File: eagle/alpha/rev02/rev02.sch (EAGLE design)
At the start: 311 parts, among them CN1 HOST, IC3 N25Q128A13ES, Q3 2N7002, Q5 ASFL1, Q6 2N7002, T1 BC847, T2 BC847, T3 BC818, U1 LP3985IM5-3.3, U2 MC74HC1G14DTT1G, U3 ATTINY828R-AU, U4 MC14551BDG, U5 23K640-I/SN, U6 MCP79412-I/SN, U7 XC7A200TFBG484, Y1 12 MHz

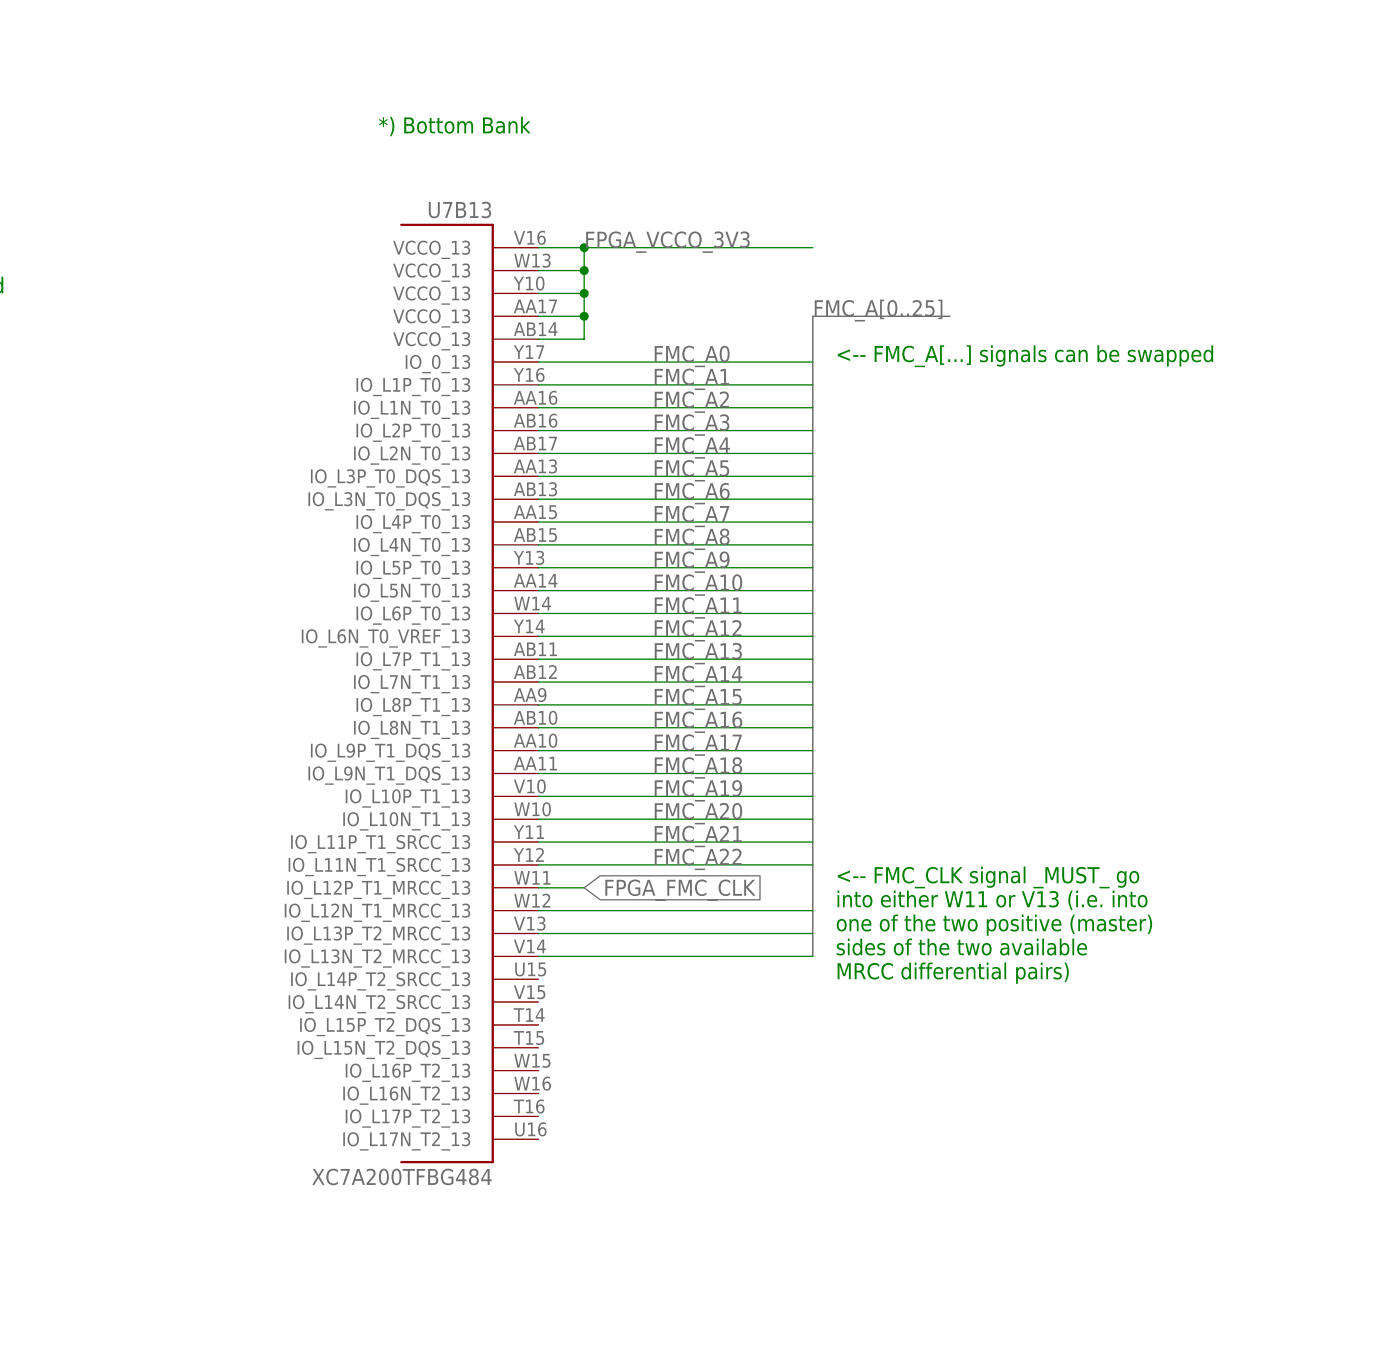
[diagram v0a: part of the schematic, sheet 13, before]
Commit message: finished merging Pavel's FPGA schematics into the dev-bridge schematics.
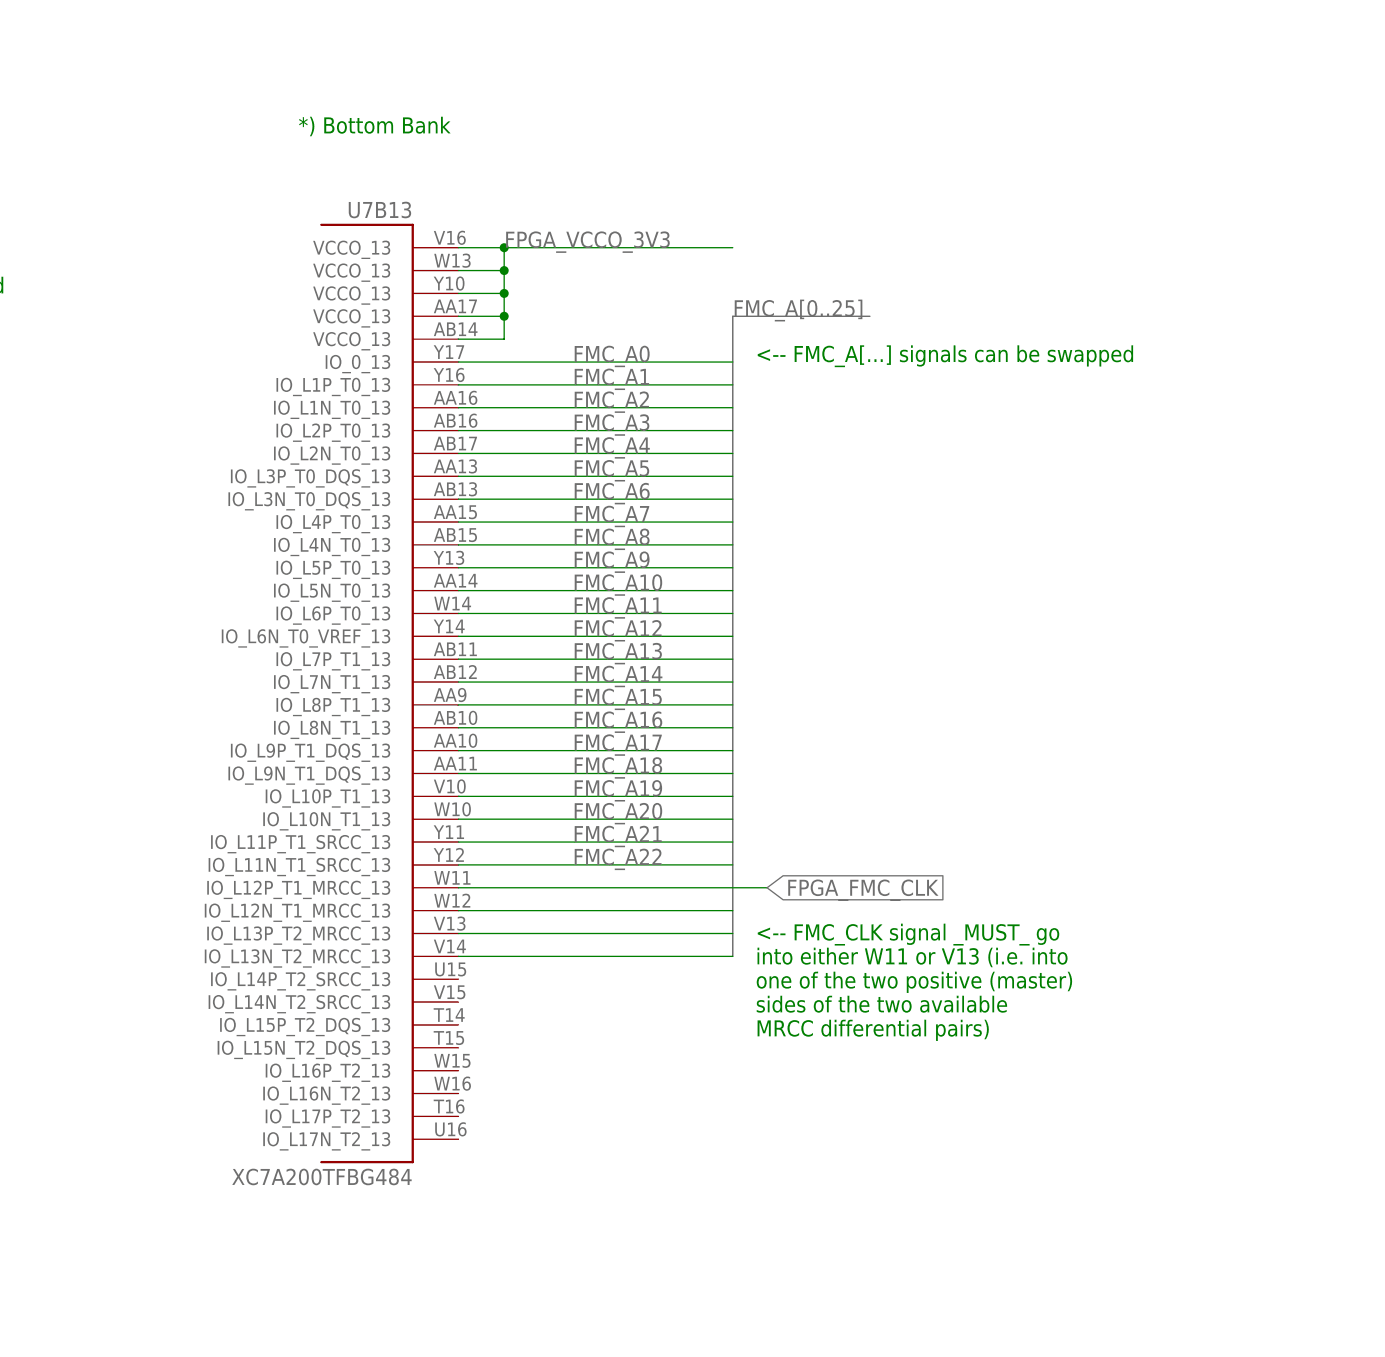
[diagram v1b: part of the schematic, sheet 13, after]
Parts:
- added C1, C4: 10NF, rcl:C-EUC0603
- added U$9: LT3060, Alpha-Power:LT3060
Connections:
- removed net DIGITIZED: U2.OUT_Y
- removed net FMC_CLK: U$1G$4.PD3/FMC_CLK
- removed net FPGA_PROM_CS_B: U7B14.IO_L6P_T0_FCS_B_14
- new net FPGA_ENTROPY_ENABLE: U$9.!SHDN
- new net N$1: C1.1, U$9.ADJ
- new net N$2: C4.2, U$9.REF/BYP
- net 15V_STABLE: now also C1.2, U$9.OUT
- net DIGITIZED_NOISE: now also U2.OUT_Y
- net FPGA_FMC_CLK: now also U$1G$4.PD3/FMC_CLK
- net FPGA_GPIO_TAMPER_0: now also U$1G$4.PG14/FMC_A25
- net FPGA_GPIO_TAMPER_1: now also U$1G$4.PG13/FMC_A24
- net FPGA_IRQ_N_0: now also U$1G$4.PG12/FMC_NE4
- net FPGA_IRQ_N_1: now also U$1G$4.PG11/FMC_NCE4_2
- net FPGA_IRQ_N_2: now also U$1G$4.PG10/FMC_NCE4_1/FMC_NE3
- net FPGA_IRQ_N_3: now also U$1G$4.PG9/FMC_NE2/FMC_NCE3
- net FPGA_PROM_CS_N: now also U7B14.IO_L6P_T0_FCS_B_14
- net GND: now also C4.1, U$9.GND
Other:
- note added: "*) FPGA_GPIO_* and FPGA_IRQ_N_* signals can be swapped with any other available GPIO on the ARM"
- note added: "FPGA_DONE can be swapped with any other available GPIO pin on the ARM"
- note added: "XXX FPGA_INIT_B unconnected?"
- note added: "XXX add optocoupler as per Jacob's suggestion on tech@ 2015-07-24?"
- note added: "XXX typo? Was FPGA_PROM_CS_B"
- note added: "XXX what to use for LowESR caps?"
- note added: "XXX where to connect FPGA_ENTROPY_ENABLE?"
- note removed: "XXX FPGA_JTAG_TDO not connected?"
- note removed: "XXX add 15V LDO for noise source"
- moved on the sheet: C133, JP1, U$7, U$8, U7B13

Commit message: lots of updates after call with Pavel
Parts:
- removed C10: 1.0 uF, microbuilder:CAP_CERAMIC0805
- removed C12: 10 uF, microbuilder:CAP_CERAMIC0805
- removed C8: 10NF, rcl:C-EUC0603
- removed U1: LP3985IM5-3.3, LP3985IM5:LP3985IM5-3.3
- added C5: 2.2 uF LowESR, resistor:C-EUC0603
- added C6: 0.1uF, resistor:C-EUC0402
- added JP2: (no value), SparkFun-Connectors:M03LOCK
- added R22: 10K, resistor:R-EU_R0402
- C1, C4: device rcl:C-EUC0603 -> rcl:C-EUC0402; RATED_VOLTAGE (none) -> 25V
- C14, C15: device rcl:C-EUC0603 -> rcl:C-EUC0402
- C16, C17: device microbuilder:CAP_CERAMIC0805 -> resistor:C-EUC0805
- C18, C19, C20, C21, C22, C23, C24, C26, C27, C31, C32, C33, C34, C35, C36, C37: device microbuilder:CAP_CERAMIC0603 -> resistor:C-EUC0402; RATED_VOLTAGE 50V -> 10V
- C25, C28, C29, C41, C42, C46, C48, C49, C51, C53, C54, C55: device microbuilder:CAP_CERAMIC0603 -> resistor:C-EUC0402
- C30, C45, C47: device microbuilder:CAP_CERAMIC0603 -> resistor:C-EUC0603
- C38, C39, C56, C57: device microbuilder:CAP_CERAMIC0603 -> resistor:C-EUC0603; DIELECTRIC (none) -> X7R; RATED_VOLTAGE (none) -> 10V
- C40: device microbuilder:CAP_CERAMIC0603 -> resistor:C-EUC0402; DIELECTRIC (none) -> X7R; RATED_VOLTAGE (none) -> 10V
- C43, C44: DIELECTRIC (none) -> C0G; RATED_VOLTAGE (none) -> 10V
- C50, C52: device microbuilder:CAP_CERAMIC_0805 -> resistor:C-EUC0805
- C58: value 10 uF X7R 10v -> 10 uF; device microbuilder:CAP_CERAMIC0805 -> resistor:C-EUC0805; DIELECTRIC (none) -> X7R; RATED_VOLTAGE (none) -> 10V
- C59, C60, C61, C62: value 0.1 uF X7R 10v -> 0.1 uF; device microbuilder:CAP_CERAMIC0603 -> resistor:C-EUC0402; DIELECTRIC (none) -> X7R; RATED_VOLTAGE (none) -> 10V
- C7: value 1.0 uF -> 0.1 uF; device microbuilder:CAP_CERAMIC0805 -> resistor:C-EUC0402; RATED_VOLTAGE (none) -> 10V
- LED1, LED5: value B -> BLUE
- LED10, LED2, LED6: value G -> GREEN
- LED15, LED4, LED8: value R -> RED
- LED16: value (none) -> GREEN
- LED3, LED7, LED9: value Y -> YELLOW
- R10, R11, R12, R13, R14, R15, R16: device resistor:R-EU_R0603 -> resistor:R-EU_R0402
- U$9: value LT3060 -> LT3060ITS8-15; device Alpha-Power:LT3060 -> Alpha-Power:LT3060ITS8-15
- Y1: MPN (none) -> ABM8G-12.000MHZ-4Y-T3; OC_FARNELL (none) -> 2467837; SUPPLIER (none) -> ABRACON
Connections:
- net !MKM_CS renamed MKM_CS_N
- net MKM_AVR_CS renamed MKM_AVR_CS_N
- net MKM_FPGA_CS renamed MKM_FPGA_CS_N
- removed net 3V3: C13.2, C16.P$1, C17.P$1, C18.P$1, C19.P$1, C20.P$1, C21.P$1, C22.P$1, C23.P$1, C24.P$1, C25.P$1, C26.P$1, C27.P$1, C28.P$1, C29.P$1, C30.P$1, C31.P$1, C32.P$1, C33.P$1, C34.P$1, C35.P$1, C36.P$1, C37.P$1, C38.P$1, C39.P$1, C56.P$1, C57.P$1, C7.P$1, JP6.1, R1.2, U$1G$1.VBAT@6, U$1G$1.VDD@15, U$1G$1.VDD@26, U$1G$1.VDD@39, U$1G$1.VDD@52, U$1G$1.VDDA@42, U$1G$1.VREF+@41, U$1G$2.VDD@103, U$1G$2.VDD@59, U$1G$2.VDD@73, U$1G$2.VDD@83, U$1G$2.VDD@94, U$1G$3.VDD@115, U$1G$3.VDD@124, U$1G$3.VDD@137, U$1G$3.VDD@150, U$1G$4.PDR_ON@203, U$1G$4.VDD@158, U$1G$4.VDD@171, U$1G$4.VDD@185, U$1G$4.VDD@204, U$2.VCC, U1.VOUT, U2.VCC, U6.VCC
- removed net FPGA_VCCO_3V3: C100.1, C101.1, C102.1, C105.1, C106.1, C107.1, C108.1, C109.1, C110.1, C113.1, C117.1, C118.1, C119.1, C120.1, C121.1, C122.1, C123.1, C124.1, C125.1, C126.1, C127.1, C128.1, C129.1, C133.1, C134.1, C135.1, C136.1, C156.1, C157.1, C158.1, C159.1, C160.1, C161.1, C162.1, C163.1, C164.1, C165.1, C166.1, C167.1, C170.1, C171.1, C172.1, C173.1, C97.1, C98.1, IC3.!HOLD!/DQ3, IC3.VCC, JP7.2, Q5.VCC, R25.2, R26.2, R27.2, R28.2, R33.2, R35.2, R36.2, R37.2, R49.2, R9.2, SV1.1, SV1.2, SV1.3, SV1.4, SV2.1, SV2.2, SV2.3, SV2.4, SV3.1, U7B0.CFGBVS_0, U7B0.VCCO_0@0, U7B0.VCCO_0@1, U7B13.VCCO_13@0, U7B13.VCCO_13@1, U7B13.VCCO_13@2, U7B13.VCCO_13@3, U7B13.VCCO_13@4, U7B14.VCCO_14@0, U7B14.VCCO_14@1, U7B14.VCCO_14@2, U7B14.VCCO_14@3, U7B14.VCCO_14@4, U7B14.VCCO_14@5, U7B15.VCCO_15@0, U7B15.VCCO_15@1, U7B15.VCCO_15@2, U7B15.VCCO_15@3, U7B15.VCCO_15@4, U7B15.VCCO_15@5, U7B16.VCCO_16@0, U7B16.VCCO_16@1, U7B16.VCCO_16@2, U7B16.VCCO_16@3, U7B16.VCCO_16@4, U7B16.VCCO_16@5, U7B34.VCCO_34@0, U7B34.VCCO_34@1, U7B34.VCCO_34@2, U7B34.VCCO_34@3, U7B34.VCCO_34@4, U7B34.VCCO_34@5, U7B35.VCCO_35@0, U7B35.VCCO_35@1, U7B35.VCCO_35@2, U7B35.VCCO_35@3, U7B35.VCCO_35@4, U7B35.VCCO_35@5
- removed net N$8: C8.2, U1.BYPASS
- removed net VPGA_VCCO_3V3: R24.2
- new net 15V_LDO_ENABLE: JP2.2, R22.2, U$9.!SHDN
- new net FT_CTS: U$3.CTS#
- new net FT_DTR: U$3.DTR#
- new net FT_RTS: U$3.RTS#
- new net VCC: C7.1, JP5.1
- new net VCCO_3V3: C100.1, C101.1, C102.1, C105.1, C106.1, C107.1, C108.1, C109.1, C110.1, C113.1, C117.1, C118.1, C119.1, C120.1, C121.1, C122.1, C123.1, C124.1, C125.1, C126.1, C127.1, C128.1, C129.1, C13.2, C133.1, C134.1, C135.1, C136.1, C156.1, C157.1, C158.1, C159.1, C16.1, C160.1, C161.1, C162.1, C163.1, C164.1, C165.1, C166.1, C167.1, C17.1, C170.1, C171.1, C172.1, C173.1, C18.1, C19.1, C20.1, C21.1, C22.1, C23.1, C24.1, C25.1, C26.1, C27.1, C28.1, C29.1, C30.1, C31.1, C32.1, C33.1, C34.1, C35.1, C36.1, C37.1, C38.1, C39.1, C56.1, C57.1, C6.1, C97.1, C98.1, IC3.!HOLD!/DQ3, IC3.VCC, JP6.1, JP7.2, Q5.VCC, R1.2, R24.2, R25.2, R26.2, R27.2, R28.2, R33.2, R35.2, R36.2, R37.2, R49.2, R9.2, SV1.1, SV1.2, SV1.3, SV1.4, SV2.1, SV2.2, SV2.3, SV2.4, SV3.1, U$1G$1.VBAT@6, U$1G$1.VDD@15, U$1G$1.VDD@26, U$1G$1.VDD@39, U$1G$1.VDD@52, U$1G$1.VDDA@42, U$1G$1.VREF+@41, U$1G$2.VDD@103, U$1G$2.VDD@59, U$1G$2.VDD@73, U$1G$2.VDD@83, U$1G$2.VDD@94, U$1G$3.VDD@115, U$1G$3.VDD@124, U$1G$3.VDD@137, U$1G$3.VDD@150, U$1G$4.PDR_ON@203, U$1G$4.VDD@158, U$1G$4.VDD@171, U$1G$4.VDD@185, U$1G$4.VDD@204, U$2.VCC, U2.VCC, U6.VCC, U7B0.CFGBVS_0, U7B0.VCCO_0@0, U7B0.VCCO_0@1, U7B13.VCCO_13@0, U7B13.VCCO_13@1, U7B13.VCCO_13@2, U7B13.VCCO_13@3, U7B13.VCCO_13@4, U7B14.VCCO_14@0, U7B14.VCCO_14@1, U7B14.VCCO_14@2, U7B14.VCCO_14@3, U7B14.VCCO_14@4, U7B14.VCCO_14@5, U7B15.VCCO_15@0, U7B15.VCCO_15@1, U7B15.VCCO_15@2, U7B15.VCCO_15@3, U7B15.VCCO_15@4, U7B15.VCCO_15@5, U7B16.VCCO_16@0, U7B16.VCCO_16@1, U7B16.VCCO_16@2, U7B16.VCCO_16@3, U7B16.VCCO_16@4, U7B16.VCCO_16@5, U7B34.VCCO_34@0, U7B34.VCCO_34@1, U7B34.VCCO_34@2, U7B34.VCCO_34@3, U7B34.VCCO_34@4, U7B34.VCCO_34@5, U7B35.VCCO_35@0, U7B35.VCCO_35@1, U7B35.VCCO_35@2, U7B35.VCCO_35@3, U7B35.VCCO_35@4, U7B35.VCCO_35@5
- net 15V_STABLE: now also C5.1
- net 3V3_BATT: now also C58.1, C59.1, C60.1, C61.1, C62.1; no longer C58.P$1, C59.P$1, C60.P$1, C61.P$1, C62.P$1, JP5.1
- net FPGA_ENTROPY_ENABLE: now also JP2.1; no longer U$9.!SHDN
- net FPGA_GPIO_TAMPER_0: now also U3.PB6_(PCINT14/ADC14); no longer U$1G$4.PG14/FMC_A25
- net FPGA_GPIO_TAMPER_1: now also U3.PB7_(PCINT15/ADC15); no longer U$1G$4.PG13/FMC_A24
- net FPGA_INIT_B: now also U$1G$4.PJ14
- net FPGA_PROGRAM_B: now also U$1G$4.PJ15
- net FT_VCC3V3: now also C47.1, C48.1, C53.1, C54.1, C55.1; no longer C47.P$1, C48.P$1, C53.P$1, C54.P$1, C55.P$1
- net FT_VCCA: now also C41.1; no longer C41.P$1
- net FT_VCCORE: now also C42.1; no longer C42.P$1
- net FT_VPHY: now also C49.1, C50.1; no longer C49.P$1, C50.P$1
- net FT_VPLL: now also C51.1, C52.1; no longer C51.P$1, C52.P$1
- net FT_VREGIN: now also C45.1, C46.1; no longer C45.P$1, C46.P$1
- net GND: now also C16.2, C17.2, C18.2, C19.2, C20.2, C21.2, C22.2, C23.2, C24.2, C25.2, C26.2, C27.2, C28.2, C29.2, C30.2, C31.2, C32.2, C33.2, C34.2, C35.2, C36.2, C37.2, C40.2, C41.2, C42.2, C45.2, C46.2, C47.2, C48.2, C49.2, C5.2, C50.2, C51.2, C52.2, C53.2, C54.2, C55.2, C58.2, C59.2, C6.2, C60.2, C61.2, C62.2, C7.2, U$8.AGND; no longer C10.P$2, C12.P$2, C16.P$2, C17.P$2, C18.P$2, C19.P$2, C20.P$2, C21.P$2, C22.P$2, C23.P$2, C24.P$2, C25.P$2, C26.P$2, C27.P$2, C28.P$2, C29.P$2, C30.P$2, C31.P$2, C32.P$2, C33.P$2, C34.P$2, C35.P$2, C36.P$2, C37.P$2, C40.P$2, C41.P$2, C42.P$2, C45.P$2, C46.P$2, C47.P$2, C48.P$2, C49.P$2, C50.P$2, C51.P$2, C52.P$2, C53.P$2, C54.P$2, C55.P$2, C58.P$2, C59.P$2, C60.P$2, C61.P$2, C62.P$2, C7.P$2, C8.1, U$8.AGND@5, U$8.AGND@6, U1.GND
- net NRST: now also C40.1; no longer C40.P$1
- net PWR_18V: now also R22.1, U$8.VIN, U$9.IN; no longer U$8.VIN@1, U$8.VIN@2
- net VCAP1: now also C39.2, C56.2; no longer C39.P$2, C56.P$2
- net VCAP2: now also C38.2, C57.2; no longer C38.P$2, C57.P$2
- net VCC_5V0: now also U$8.VOUT; no longer C10.P$1, C12.P$1, U$8.VOUT@10, U$8.VOUT@11, U1.VEN, U1.VIN
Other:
- note added: "*) FPGA_GPIO_*, FPGA_IRQ_N_* and FPGA_{PROGRAM,INIT}_B signals can be swapped with any other available GPIO on the ARM"
- note added: "15V LDO powered from external 18V and supplying stable 15V to noise source"
- note added: "2*2.2uF LowESR or 1*4.7uF LowESR < 1 ohm (ST AN4488 §2.2)"
- note added: "AVR_GPIO* AVR_LED*, AVR_PANIC and FPGA_GPIO_TAMPER* can be swapped."
- note added: "Add optocoupler as per Jacob's suggestion on tech@ 2015-07-24? The suggestion is to add a fast optocoupler to really isolate AGND from GND. As this appears to require a bigger digitizer, we are reluctant to add that for the Alpha."
- note added: "Do we need more speed? Joachim expressed that we might need a faster interconnect to the Alpha than the 12 Mbaud the FT232H can deliver in UART mode (in an e-mail to tech@ 2015-08-18). An alternative is to connect all of the ADBUS (and more) to the ARM, and use one of the faster modes this chip supports (fastest: synchronous FT245 parallel FIFO at 40 Mbyte/s). Enabling the faster modes requires t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"
- note added: "Jumper deciding if FPGA/ARM/None should be allowed to turn off the entropy source (default On through pull-up)"
- note added: "Main power input 18V DC"
- note added: "Max 3 ohm ESR"
- note added: "PDR_ON high enables internal power regulator"
- note added: "Place a jumper between pins 1-2 to "emulate" having a battery present."
- note added: "ST AN8844 §2.2 One bypass capacitor for every VDD. Use 0.1 uF X7R (X5R?) 10V."
- note added: "THESE TWO TO AT TINY"
- note added: "This is the 3V3 rail that powers both the FPGA and the ARM as well as various other components."
- note added: "This page intentionally left blank"
- note added: "XXX FPGA_INIT_B should go to ARM GPIO? What is PROG_B?"
- note added: "XXX test this circuit"
- note removed: "(routed via bottom layer in case pull-up is needed)"
- note removed: "*) FPGA_GPIO_* and FPGA_IRQ_N_* signals can be swapped with any other available GPIO on the ARM"
- note removed: "2*2.2uF LowESR or 1*4.7uF LowESR (ST 4488 §2.2)"
- note removed: "Enable internal power regulator"
- note removed: "Main power input 18V"
- note removed: "Output cap should be X7R with ESR between 5-500 mOhm."
- note removed: "ST AN8844 §2.2 One bypass capacitor for every VDD. Use 0.1 uF X7R 50V."
- note removed: "VCC 3.3V regulator powering ARM etc. (but not the FPGA)"
- note removed: "XXX FPGA_INIT_B unconnected?"
- note removed: "XXX add optocoupler as per Jacob's suggestion on tech@ 2015-07-24?"
- note removed: "XXX typo? Was FPGA_PROM_CS_B"
- note removed: "XXX what to use for LowESR caps?"
- note removed: "XXX where to connect FPGA_ENTROPY_ENABLE?"

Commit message: add more parts of the schematic (SRAM, analog switch for config mem)
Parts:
- added C8: 0.1 uF, resistor:C-EUC0402
- added IC1: IS45S32160F, Alpha-IC:IS45S32160F
- added JP8: (no value), jumper:JP1Q
- added R30, R31, R6: 10K, resistor:R-EU_R0402
- added R32: 15K, resistor:R-EU_R0603
- added U1: MC14551BDG, ON_Semiconductor-MC14551BDG:MC14551BDG
- LED11: value (none) -> BLUE
- LED12: value (none) -> GREEN
- LED13: value (none) -> YELLOW
- LED14: value (none) -> RED
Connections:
- new net ARM_FPGA_CFG_CONTROL: JP8.2, U$1G$4.PD2
- new net ARM_FPGA_CFG_CS_N: U1.X1
- new net ARM_FPGA_CFG_MISO: U$1G$4.PC11/SPI3_MISO, U1.W1
- new net ARM_FPGA_CFG_MOSI: U$1G$4.PC12/SPI3_MOSI, U1.Y1
- new net ARM_FPGA_CFG_SCLK: U$1G$4.PC10/SPI3_SCK, U1.Z1
- new net FPGA_CFG_CS_N: U1.X, U7B14.IO_L6P_T0_FCS_B_14
- new net FPGA_CFG_MISO: U1.W, U7B14.IO_L1N_T0_D01_DIN_14
- new net FPGA_CFG_MOSI: U1.Y, U7B14.IO_L1P_T0_D00_MOSI_14
- new net FPGA_CFG_SCLK: U1.Z, U7B0.CCLK_0
- new net N$3: JP8.1, R32.2, U1.CONTROL
- net 3V3_BATT: now also C8.1, U1.VDD
- net FMC_D0: now also IC1.DQ0
- net FMC_D1: now also IC1.DQ1
- net FMC_D10: now also IC1.DQ10
- net FMC_D11: now also IC1.DQ11
- net FMC_D12: now also IC1.DQ12
- net FMC_D13: now also IC1.DQ13
- net FMC_D14: now also IC1.DQ14
- net FMC_D15: now also IC1.DQ15
- net FMC_D16: now also IC1.DQ16
- net FMC_D17: now also IC1.DQ17
- net FMC_D18: now also IC1.DQ18, IC1.DQ19
- net FMC_D2: now also IC1.DQ2
- net FMC_D20: now also IC1.DQ20
- net FMC_D21: now also IC1.DQ21
- net FMC_D22: now also IC1.DQ22
- net FMC_D23: now also IC1.DQ23
- net FMC_D24: now also IC1.DQ24
- net FMC_D25: now also IC1.DQ25
- net FMC_D26: now also IC1.DQ26
- net FMC_D27: now also IC1.DQ27
- net FMC_D28: now also IC1.DQ28
- net FMC_D29: now also IC1.DQ29
- net FMC_D3: now also IC1.DQ3
- net FMC_D30: now also IC1.DQ30
- net FMC_D31: now also IC1.DQ31
- net FMC_D4: now also IC1.DQ4
- net FMC_D5: now also IC1.DQ5
- net FMC_D6: now also IC1.DQ6
- net FMC_D7: now also IC1.DQ7
- net FMC_D8: now also IC1.DQ8
- net FMC_D9: now also IC1.DQ9
- net FPGA_PROM_CS_N: now also U1.X0; no longer U7B14.IO_L6P_T0_FCS_B_14
- net FPGA_PROM_MISO: now also U1.W0; no longer U7B14.IO_L1N_T0_D01_DIN_14
- net FPGA_PROM_MOSI: now also U1.Y0; no longer U7B14.IO_L1P_T0_D00_MOSI_14
- net FPGA_PROM_SCLK: now also U1.Z0; no longer U7B0.CCLK_0
- net GND: now also C8.2, R32.1, U1.VEE, U1.VSS
- net RTC_MFP: now also R6.2
- net RTC_SCL: now also R30.2, U$1G$1.I2C2_SCL/PH4; no longer U$1G$1.PH4
- net RTC_SDA: now also R31.2, U$1G$1.I2C2_SDA/FMC_SDNWE/PH5; no longer U$1G$1.FMC_SDNWE/PH5
- net VCC: now also R30.1, R31.1, R6.1
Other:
- note added: "Analog switch to boot FPGA from config memory, or from ARM"
- note added: "Another identical SRAM chip goes here"
- note added: "FPGA clock"
- note added: "FPGA config memory"
- note added: "Install this jumper to allow ARM to configure the FPGA"
- note added: "Keystore memory (>= 8 MByte) goes here"
- note added: "MFP is Multi Function Pin. GPIO output from RTC."
- note added: "Micro SD card goes here"
- note added: "Pull-down CONTROL to enable 0 (PROM) by default"
- note added: "Real Time Clock"
- note added: "XXX are jumpers on the ARM SPI nets really needed, when CONTROL defaults to the PROM?"
- note added: "i2c pull-ups, typically 10K for 100kHz"
- note removed: "XXX FPGA_INIT_B should go to ARM GPIO? What is PROG_B?"
